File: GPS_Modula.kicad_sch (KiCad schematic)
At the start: 17 parts, among them J3 Conn_Coaxial, U11 AMS1117-3.3, U2 NEO-M8M, U5 AT24CS01-XHM

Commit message: mostly layouted
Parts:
- D2: footprint Diode_THT:D_DO-35_SOD27_P7.62mm_Horizontal -> Diode_SMD:D_SOD-323
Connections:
- net GND: no longer TP19.1
- net PSU: now also TP19.1
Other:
- moved on the sheet: TP19
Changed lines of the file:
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@@
+		)
+	)
+	(wire
+		(pts
+			(xy 170.18 29.21) (xy 170.18 31.75)
+		)
+		(stroke
+			(width 0)
+			(type default)
 		)
 	)
@@
 	(symbol
 		(lib_id "Connector:TestPoint")
-		(at 170.18 39.37 180)
+		(at 170.18 29.21 0)
 		(unit 1)
 		(exclude_from_sim no)
@@
 		(fields_autoplaced yes)
 		(property "Reference" "TP19"
-			(at 172.72 41.4019 0)
-			(effects
-				(font
-					(size 1.27 1.27)
-				)
-				(justify right)
+			(at 172.72 24.6379 0)
+			(effects
+				(font
+					(size 1.27 1.27)
+				)
+				(justify left)
 			)
 		)
 		(property "Value" "TestPoint"
-			(at 172.72 43.9419 0)
-			(effects
-				(font
-					(size 1.27 1.27)
-				)
-				(justify right)
+			(at 172.72 27.1779 0)
+			(effects
+				(font
+					(size 1.27 1.27)
+				)
+				(justify left)
 			)
 		)
 		(property "Footprint" "TestPoint:TestPoint_Pad_D2.0mm"
-			(at 165.1 39.37 0)
+			(at 175.26 29.21 0)
 			(effects
 				(font
@@
 		)
 		(property "Datasheet" "~"
-			(at 165.1 39.37 0)
+			(at 175.26 29.21 0)
 			(effects
 				(font
@@
 		)
 		(property "Description" "test point"
-			(at 170.18 39.37 0)
+			(at 170.18 29.21 0)
 			(effects
 				(font
@@
 		)
 		(property "Availability" ""
-			(at 170.18 39.37 0)
+			(at 170.18 29.21 0)
 			(effects
 				(font
@@
 		)
 		(property "Check_prices" ""
-			(at 170.18 39.37 0)
+			(at 170.18 29.21 0)
 			(effects
 				(font
@@
 		)
 		(property "Description_1" ""
-			(at 170.18 39.37 0)
+			(at 170.18 29.21 0)
 			(effects
 				(font
@@
 		)
 		(property "MANUFACTURER" ""
-			(at 170.18 39.37 0)
+			(at 170.18 29.21 0)
 			(effects
 				(font
@@
 		)
 		(property "MAXIMUM_PACKAGE_HEIGHT" ""
-			(at 170.18 39.37 0)
+			(at 170.18 29.21 0)
 			(effects
 				(font
@@
 		)
 		(property "MF" ""
-			(at 170.18 39.37 0)
+			(at 170.18 29.21 0)
 			(effects
 				(font
@@
 		)
 		(property "MP" ""
-			(at 170.18 39.37 0)
+			(at 170.18 29.21 0)
 			(effects
 				(font
@@
 		)
 		(property "PARTREV" ""
-			(at 170.18 39.37 0)
+			(at 170.18 29.21 0)
 			(effects
 				(font
@@
 		)
 		(property "Package" ""
-			(at 170.18 39.37 0)
+			(at 170.18 29.21 0)
 			(effects
 				(font
@@
 		)
 		(property "Price" ""
-			(at 170.18 39.37 0)
+			(at 170.18 29.21 0)
 			(effects
 				(font
@@
 		)
 		(property "SNAPEDA_PN" ""
-			(at 170.18 39.37 0)
+			(at 170.18 29.21 0)
 			(effects
 				(font
@@
 		)
 		(property "STANDARD" ""
-			(at 170.18 39.37 0)
+			(at 170.18 29.21 0)
 			(effects
 				(font
@@
 		)
 		(property "SnapEDA_Link" ""
-			(at 170.18 39.37 0)
+			(at 170.18 29.21 0)
 			(effects
 				(font
@@
 			)
 		)
-		(property "Footprint" "Diode_THT:D_DO-35_SOD27_P7.62mm_Horizontal"
+		(property "Footprint" "Diode_SMD:D_SOD-323"
 			(at 232.41 31.75 0)
 			(effects

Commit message: pre remobing sd card
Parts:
- TP19, TP3: footprint TestPoint:TestPoint_Pad_D2.0mm -> TestPoint:TestPoint_Pad_D1.5mm
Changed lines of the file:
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@@
 			)
 		)
-		(property "Footprint" "TestPoint:TestPoint_Pad_D2.0mm"
+		(property "Footprint" "TestPoint:TestPoint_Pad_D1.5mm"
 			(at 224.79 31.75 0)
 			(effects
@@
 			)
 		)
-		(property "Footprint" "TestPoint:TestPoint_Pad_D2.0mm"
+		(property "Footprint" "TestPoint:TestPoint_Pad_D1.5mm"
 			(at 175.26 29.21 0)
 			(effects

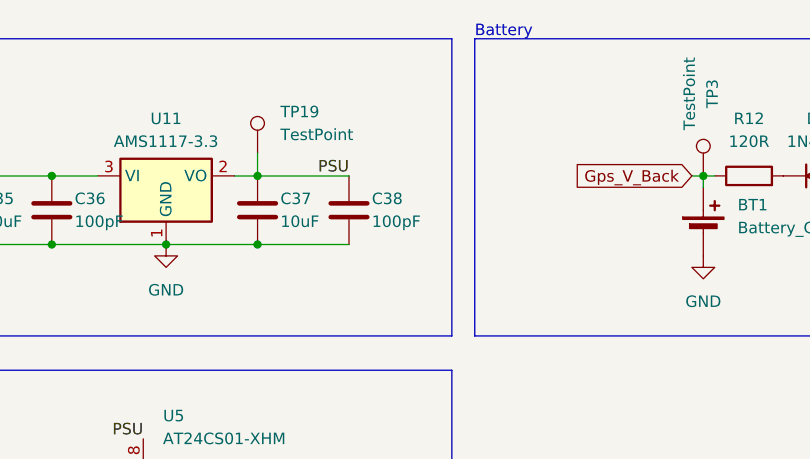
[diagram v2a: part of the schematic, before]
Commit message: switchen can supply to 3v3
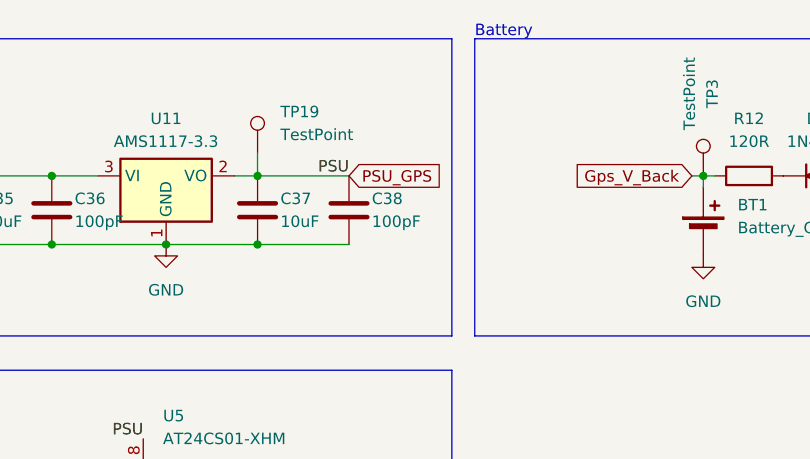
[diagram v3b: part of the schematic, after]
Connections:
- net PSU renamed PSU_GPS
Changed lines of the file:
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@@
+		)
+	)
+	(global_label "PSU_GPS"
+		(shape input)
+		(at 180.34 31.75 0)
+		(fields_autoplaced yes)
+		(effects
+			(font
+				(size 1.27 1.27)
+			)
+			(justify left)
+		)
+		(property "Intersheetrefs" "${INTERSHEET_REFS}"
+			(at 191.8523 31.75 0)
+			(effects
+				(font
+					(size 1.27 1.27)
+				)
+				(justify left)
+				(hide yes)
+			)
 		)
 	)

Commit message: first new layout
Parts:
- removed TP19, TP3: TestPoint, TestPoint:TestPoint_Pad_D1.5mm, symbol Connector:TestPoint
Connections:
- net PSU_GPS renamed +3V3
